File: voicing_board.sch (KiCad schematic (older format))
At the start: 270 parts, among them Q1 MMBT3904, Q14 MMBT3904, Q15 MMBT3904, Q16 MMBT3904, Q17 MMBT3904, Q18 MMBT3904, Q19 MMBT3904, Q2 MMBT3904, Q20 MMBT3904, Q21 MMBT3904, Q22/23 DMMT3904W, Q24 MMBT3904, Q25 MMBT3904, Q26 MMBT3904, Q27 MMBT3904, Q28 MMBT3904, Q29 MMBT3904, Q3 MMBT3904, Q30 MMBT3904, Q31 MMBT3904, Q4 MMBT3904, Q5 MMBT3906, Q6 MMBT3906, Q7 MMBT3906, Q8 MMBT3906, Q9 MMBT3904, U1 MC14584, U2 4558, U3 4558, U5 4558, U6 4558, U7 4558

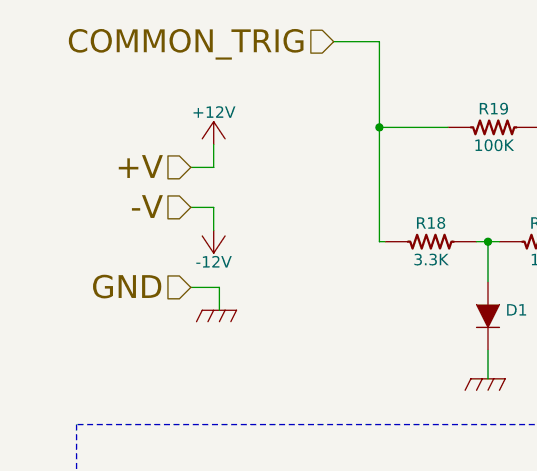
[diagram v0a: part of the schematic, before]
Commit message: updated ATMEGA328P to ATMEGA328PB. This is a newer MCU with slightly different pinout for VCC and GND. It's a little cheaper and has more timers
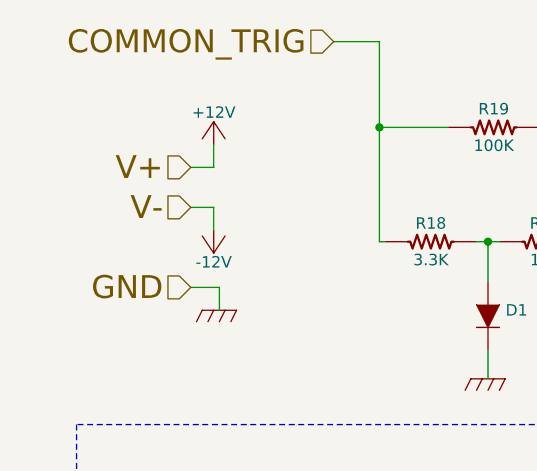
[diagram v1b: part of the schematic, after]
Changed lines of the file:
@@
 $EndComp
 Text HLabel 1150 1300 0    100  Input ~ 0
-+V
+V+
 Text HLabel 1150 1475 0    100  Input ~ 0
--V
+V-
 Text HLabel 1150 1825 0    100  Input ~ 0
 GND

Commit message: boring power decoupling added. 808 has 100R and 47uF seperate decoupling/filtering for each drum voice.
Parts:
- added C? (x8): 47μ, symbol CP_US
- added R? (x8): 100, symbol R_US
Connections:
- net +12V: now also C?.1 (+), C?.1 (+), C?.1 (+), C?.1 (+), R?.1, R?.1, R?.1, R?.1
- net -12V: now also C?.2 (-), C?.2 (-), C?.2 (-), C?.2 (-), R?.2, R?.2, R?.2, R?.2
- net GND: now also C?.1 (+), C?.1 (+), C?.1 (+), C?.1 (+), C?.2 (-), C?.2 (-), C?.2 (-), C?.2 (-)
- new net V+: R?.2, R?.2, R?.2, R?.2
- new net V-: R?.1, R?.1, R?.1, R?.1
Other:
- note added: "POWER DECOUPLING"

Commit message: housekeeping: groundng unused CMOS inputs, dealing with global and hiearchical labels
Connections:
- net TRIG renamed VB_TRIG
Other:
- note added: "POWER FILTERING\n"
- note removed: "POWER DECOUPLING"
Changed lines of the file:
@@
 $EndComp
 Text GLabel 4375 1525 2    100  Output ~ 0
-TRIG
+VB_TRIG
 Text GLabel 8125 1325 0    100  Input ~ 0
-TRIG
+VB_TRIG
 Text GLabel 10175 1325 0    100  Input ~ 0
-TRIG
+VB_TRIG
 Text GLabel 1875 2800 0    100  Input ~ 0
-TRIG
+VB_TRIG
 Text GLabel 13500 8225 2    100  Input ~ 0
-TRIG
+VB_TRIG
 $Comp
 L R_US R19
@@
 	20875 8025 17650 8025
 Text Notes 17700 8350 0    200  ~ 40
-POWER DECOUPLING
+POWER FILTERING\n
 $EndSCHEMATC

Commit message: entire project annotaed, duplicate references fixed with '-1' suffix
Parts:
- R122-1: renamed from R?; value R122 -> 1K
- gave numbers to parts that had none: 21
- renumbered C38 to C38-1, C39 to C39-1, C40 to C40-1, C41 to C41-1, C42 to C42-1, C43 to C43-1, C45 to C45-1, C47 to C47-1, C48 to C48-1, C49 to C49-1, C50 to C50-1, C51 to C51-1, C52 to C52-1, C53 to C53-1, C54 to C54-1, C55 to C55-1, C56 to C56-1, C57 to C57-1, C58 to C58-1, C59 to C59-1, C60 to C60-1, C61 to C61-1, C63 to C63-1, C65 to C65-1, C66 to C66-1, C67 to C67-1, C68 to C68-1, C69 to C69-1, C70 to C70-1, C71 to C71-1, C72 to C72-1, C72 to C73-1, C74 to C74-1, C75 to C75-1, C76 to C76-1, C77 to C77-1, C78 to C78-1, C8 to C8-1, C82 to C82-1, C83 to C83-1, C90 to C90-1, Q28 to Q28-1, Q29 to Q29-1, Q31 to Q31-1, R1 to R1-1, R10 to R10-1, R101 to R101-3, R102 to R102-1, R103 to R103-1, R104 to R104-1, R105 to R105-1, R107 to R107-1, R108 to R108-1, R11 to R11-1, R112 to R112-1, R113 to R113-1, R114 to R114-11, R117 to R117-1, R118 to R118-1, R119 to R119-1, R12 to R12-1, R120 to R120-1, R121 to R121-1, R123 to R123-1, R124 to R124-1, R128 to R128-1, R13 to R13-1, R130 to R130-1, R131 to R131-1, R132 to R132-1, R133 to R133-1, R14 to R14-1, R152 to R152-1, R153 to R153-1, R154 to R154-1, R155 to R155-1, R156 to R156-1, R157 to R157-1, R158 to R158-1, R159 to R159-1, R160 to R160-1, R161 to R161-1, R162 to R162-1, R163 to R163-1, R166 to R166-1, R169 to R169-1, R172 to R172-1, R173 to R173-1, R2 to R2-1, R3 to R3-1, R4 to R4-1, R46 to R48, R5 to R5-1, R48 to R50-1, R6 to R6-1, R7 to R7-1, R8 to R8-1, R9 to R9-1, R92 to R92-1, R93 to R93-1, R97 to R97-1, U6 to U6-1, VR4 to VR-1, VR3 to VR3-1, VR5 to VR5-1, VR6 to VR6-1, VR7 to VR7-1, VR8 to VR8-1
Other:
- note added: "C41*\n"

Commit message: netlist exported, starting footprint assignment
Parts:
- C1, C10, C11, C13, C14, C15, C16, C2, C28, C29, C3, C30, C31, C36, C4, C42-1, C43-1, C44, C46, C47-1, C48-1, C49-1, C5, C50-1, C51-1, C52-1, C53-1, C54-1, C55-1, C56-1, C57-1, C58-1, C59-1, C6, C64, C65-1, C66-1, C67-1, C68-1, C69-1, C70-1, C71-1, C72-1, C73-1, C74-1, C76-1, C77-1, C79, C80, C82-1, C90-1: footprint (none) -> MyModules:SM0603-C-JRL
- C12, C164, C165, C166, C167, C168, C169, C170, C171, C32, C33, C34, C35, C37, C38-1, C39-1, C40-1, C41-1, C45-1, C60-1, C61-1, C62, C63-1, C75-1, C78-1, C8-1, C83-1, C9: footprint (none) -> MyModules:2MM-POL-CAP
- D1, D11, D12, D13, D14, D2, D3, D4, D5, D6, D7, D8: footprint (none) -> MyModules:SOD323-C1A2

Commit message: all parts assinged except MIDI jack
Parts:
- C12: footprint MyModules:2MM-POL-CAP -> MyModules:5MM-POL-CAP
- Q1, Q14, Q15, Q16, Q17, Q18, Q19, Q2, Q20, Q21, Q22/23, Q24, Q25, Q26, Q27, Q28-1, Q29-1, Q3, Q30, Q31-1, Q4, Q5, Q6, Q7, Q8, Q9: footprint SOT-23 -> MyModules:SOT23-132-JRL
- R1-1, R10-1, R100, R101-3, R102-1, R103-1, R104-1, R105-1, R107-1, R108-1, R109, R11-1, R110, R111, R112-1, R113-1, R114-11, R115, R116, R117-1, R118-1, R119-1, R12-1, R120-1, R121-1, R122-1, R123-1, R124-1, R125, R127, R128-1, R129, R13-1, R130-1, R131-1, R132-1, R133-1, R134, R135, R136, R137, R138, R139, R14-1, R140, R141, R143, R144, R145, R146, R147, R148, R149, R15, R150, R151, R152-1, R153-1, R154-1, R155-1, R156-1, R157-1, R158-1, R159-1, R16, R160-1, R161-1, R162-1, R163-1, R166-1, R169-1, R17, R172-1, R173-1, R18, R19, R2-1, R20, R21, R22, R23, R24, R25, R26, R265, R27, R28, R29, R292, R293, R295, R3-1, R30, R31, R316, R32, R328, R329, R33, R334, R35, R357, R365, R37, R372, R379, R380, R39, R4-1, R40, R41, R42, R43, R44, R45, R46, R48, R5-1, R50-1, R52, R53, R55, R56, R58, R59, R6-1, R60, R61, R62, R63, R64, R65, R7-1, R8-1, R82, R83, R84, R85, R87, R88, R89, R9-1, R90, R91, R92-1, R93-1, R94, R95, R96, R97-1, R98, R99: footprint (none) -> MyModules:SM0603-R-JRL
- TM1, TM2: footprint (none) -> MyModules:Bourns_3362P
- TP6, TP7: footprint (none) -> MyModules:TEST_POINT_LOOP_4592
- U1: footprint (none) -> Housings_SSOP:TSSOP-14_4.4x5mm_Pitch0.65mm
- U2, U3, U5, U6-1, U7: footprint (none) -> MyModules:TSSOP8-JRL
- VR-1, VR2, VR3-1, VR5-1, VR6-1, VR7-1, VR8-1: footprint (none) -> MyModules:RD901F-ALPHA-POT
